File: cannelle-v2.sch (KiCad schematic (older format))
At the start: 30 parts, among them P1 USB_OTG, P2 CONN_02X04, U1 74LS157, U2 ATMEGA16U4-A, U3 SST25VF020B, U4 LD1117S12TR, U5 NCP1117ST33T3G, X1 8MHz

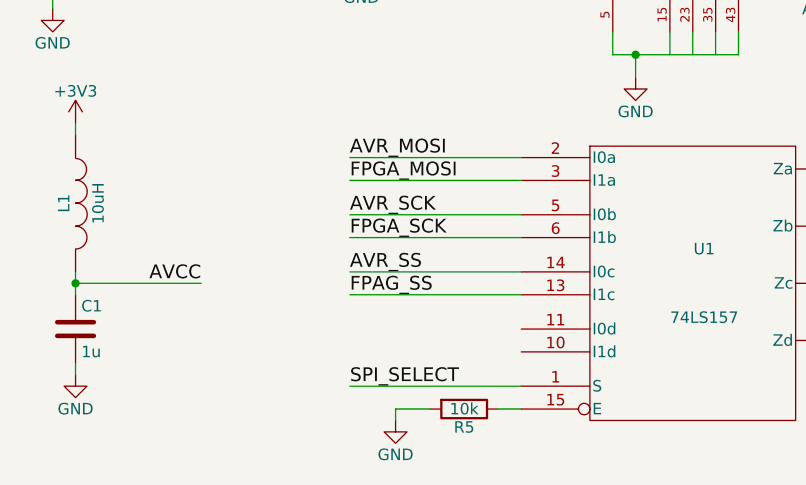
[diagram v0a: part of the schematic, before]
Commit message: Correct wrong label on schem and PCB
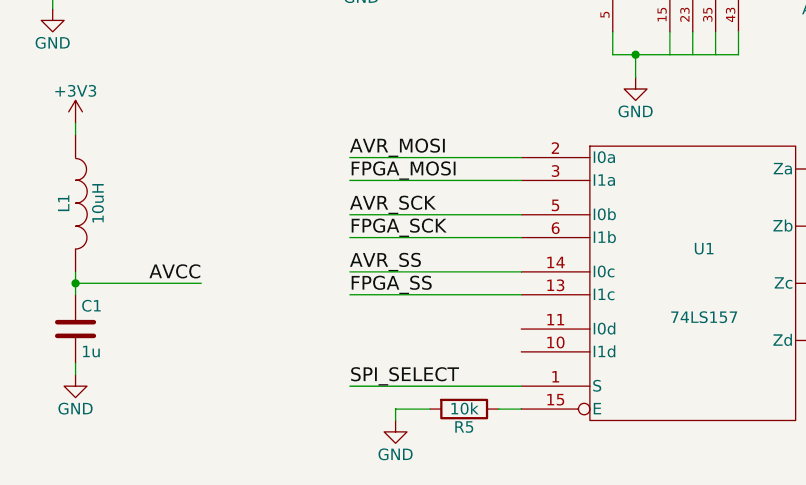
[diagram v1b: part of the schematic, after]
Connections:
- net FPAG_SS is gone; now on net FPGA_SS: U1.13 (I1c)
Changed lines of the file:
@@
 AVR_SS
 Text Label 2500 7050 0    60   ~ 0
-FPAG_SS
+FPGA_SS
 Text Label 5750 6500 2    60   ~ 0
 FLASH_MOSI

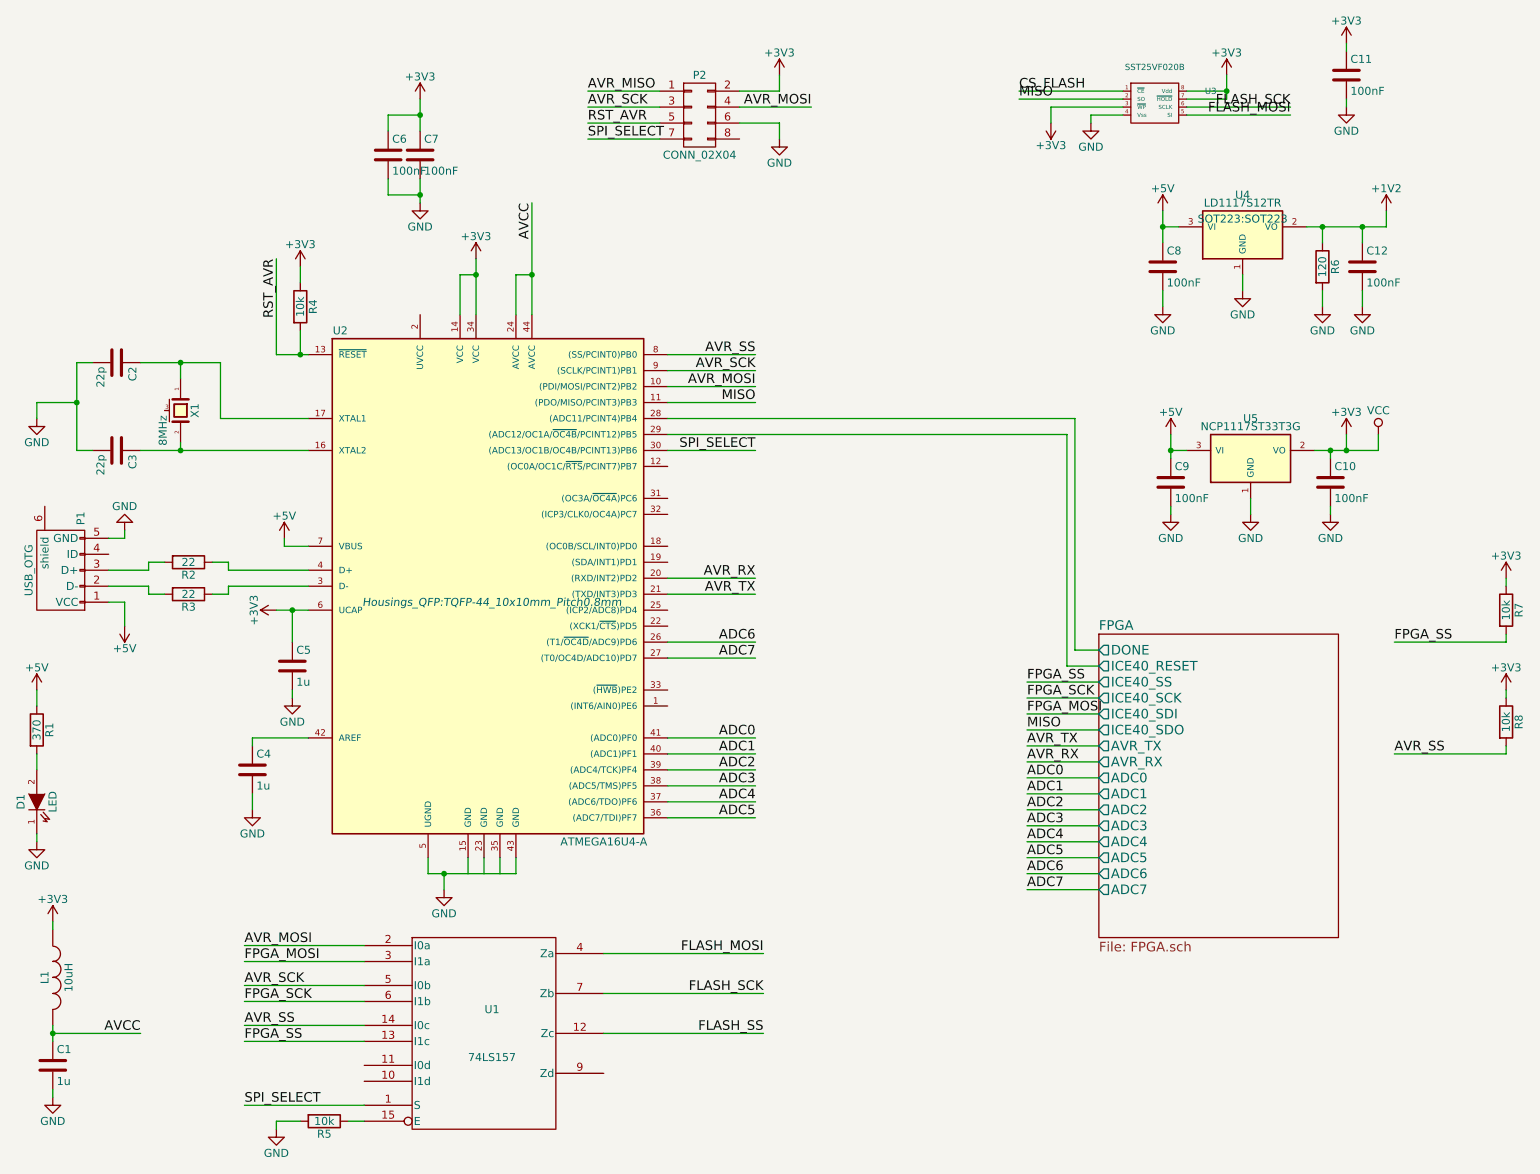
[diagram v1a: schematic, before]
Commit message: Make AtMega as only SPI Master
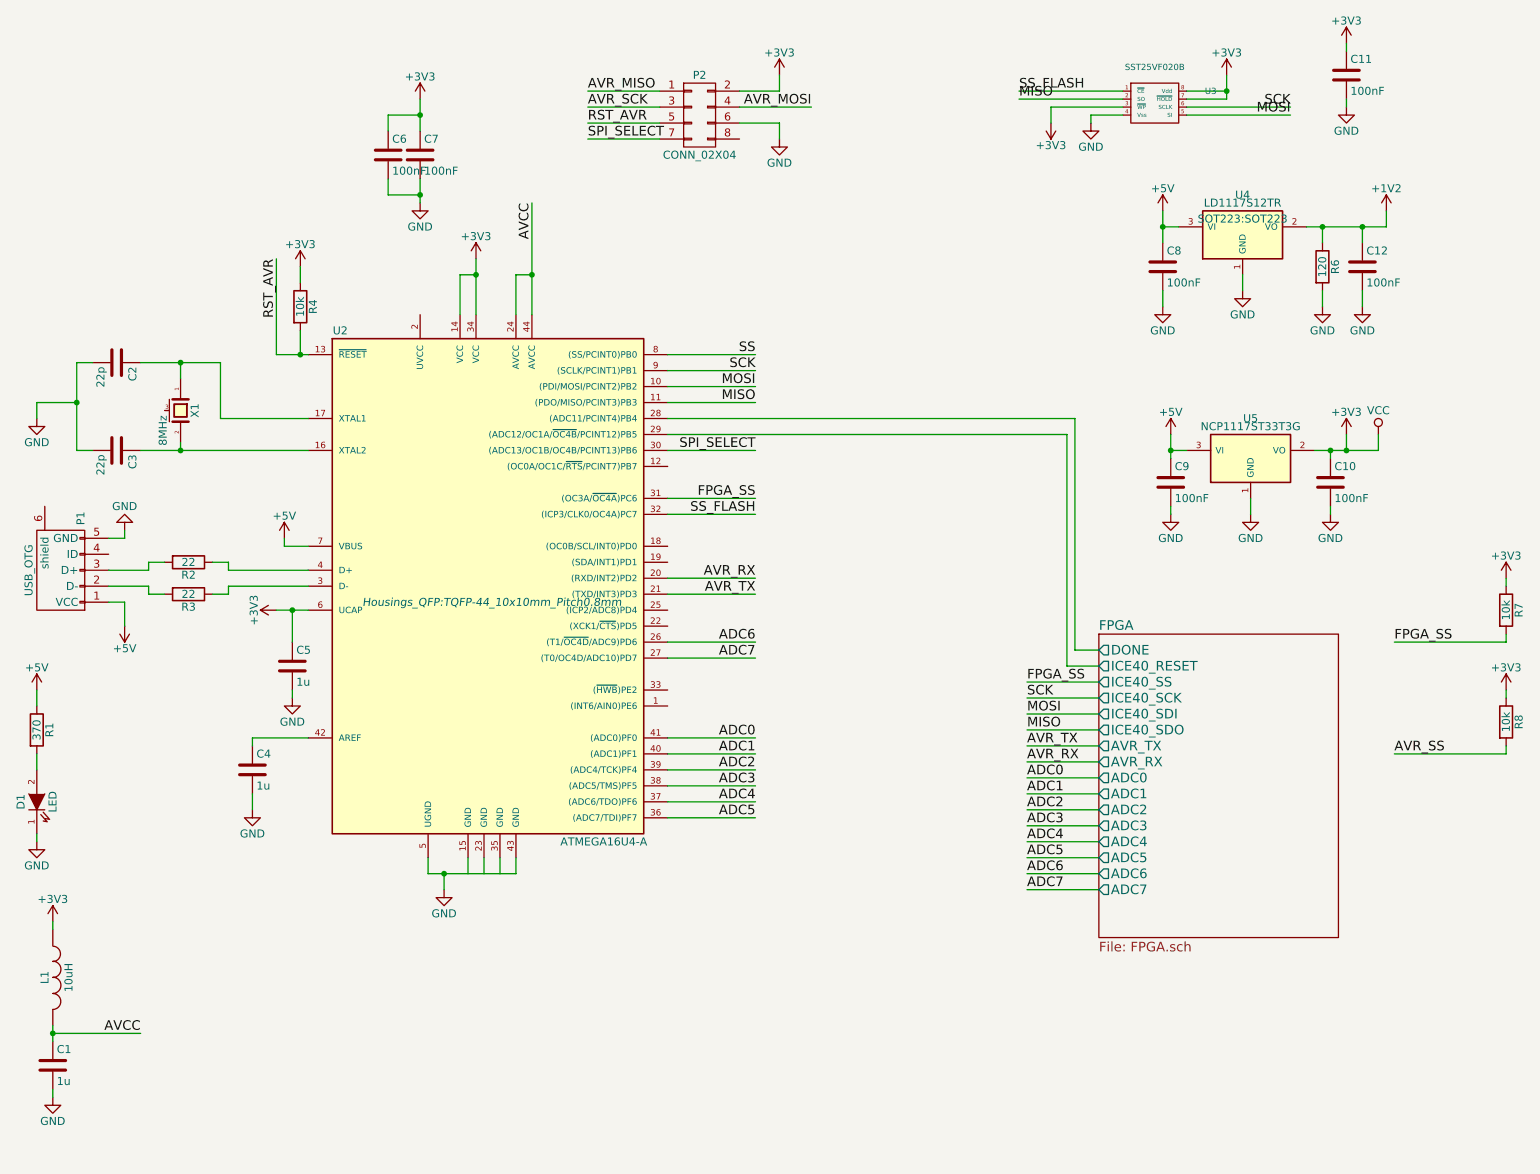
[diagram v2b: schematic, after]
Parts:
- removed R5: 10k, Resistors_SMD:R_0402, symbol R
- removed U1: 74LS157, SMD_Packages:SO-16-L, symbol 74LS157
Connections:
- net CS_FLASH is gone; now on net SS_FLASH: U3.1 (~CE)
- net AVR_MOSI: no longer U2.10 ((PDI/MOSI/PCINT2)PB2)
- net AVR_SCK: no longer U2.9 ((SCLK/PCINT1)PB1)
- net AVR_SS: no longer U2.8 ((SS/PCINT0)PB0)
- net FPGA_SS: now also U2.31 ((OC3A/~OC4A~)PC6)
- net SS_FLASH: now reaches U2.32 ((ICP3/CLK0/OC4A)PC7)
- net FLASH_MOSI renamed MOSI
- net MOSI: now also U2.10 ((PDI/MOSI/PCINT2)PB2)
- net FLASH_SCK renamed SCK
- net SCK: now also U2.9 ((SCLK/PCINT1)PB1)
- new net SS: U2.8 ((SS/PCINT0)PB0)
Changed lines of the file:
@@
 	8000 1100 7350 1100
 Text Label 7350 1100 0    60   ~ 0
-CS_FLASH
+SS_FLASH
 Wire Wire Line
 	8000 1150 7350 1150
@@
 	8400 1250 9050 1250
 Text Label 9050 1200 2    60   ~ 0
-FLASH_SCK
+SCK
 Text Label 9050 1250 2    60   ~ 0
-FLASH_MOSI
+MOSI
 Wire Wire Line
 	5150 3050 5700 3050
@@
 	5150 2950 5700 2950
 Text Label 5700 2950 2    60   ~ 0
-AVR_MOSI
+MOSI
 Wire Wire Line
 	5150 2850 5700 2850
 Text Label 5700 2850 2    60   ~ 0
-AVR_SCK
+SCK
 Wire Wire Line
 	5150 2750 5700 2750
 Text Label 5700 2750 2    60   ~ 0
-AVR_SS
+SS
 Wire Wire Line
 	5150 4150 5700 4150
@@
 FPGA_SS
 Text Label 7400 4900 0    60   ~ 0
-FPGA_SCK
+SCK
 Text Label 7400 5000 0    60   ~ 0
-FPGA_MOSI
+MOSI
 Text Label 7400 5100 0    60   ~ 0
 MISO
@@
 $EndComp
 Wire Wire Line
-	3250 6450 2500 6450
-Wire Wire Line
-	3250 6550 2500 6550
-Wire Wire Line
-	3250 6700 2500 6700
-Wire Wire Line
-	3250 6800 2500 6800
-Wire Wire Line
-	3250 6950 2500 6950
-Wire Wire Line
-	3250 7050 2500 7050
-Wire Wire Line
-	3250 7450 2500 7450
-Wire Wire Line
-	4750 6500 5750 6500
-Wire Wire Line
-	4750 6750 5750 6750
-Wire Wire Line
-	4750 7000 5750 7000
-Text Label 2500 6450 0    60   ~ 0
-AVR_MOSI
-Text Label 2500 6550 0    60   ~ 0
-FPGA_MOSI
-Text Label 2500 6700 0    60   ~ 0
-AVR_SCK
-Text Label 2500 6800 0    60   ~ 0
-FPGA_SCK
-Text Label 2500 6950 0    60   ~ 0
-AVR_SS
-Text Label 2500 7050 0    60   ~ 0
-FPGA_SS
-Text Label 5750 6500 2    60   ~ 0
-FLASH_MOSI
-Text Label 5750 6750 2    60   ~ 0
-FLASH_SCK
-Text Label 5750 7000 2    60   ~ 0
-FLASH_SS
-$Comp
-L R R5
-U 1 1 57814526
-P 3000 7550
-F 0 "R5" V 3080 7550 50  0000 C CNN
-F 1 "10k" V 3000 7550 50  0000 C CNN
-F 2 "Resistors_SMD:R_0402" V 2930 7550 50  0001 C CNN
-F 3 "" H 3000 7550 50  0000 C CNN
-	1    3000 7550
-	0    1    1    0
-$EndComp
-Wire Wire Line
-	3250 7550 3150 7550
-Wire Wire Line
-	2850 7550 2700 7550
-Wire Wire Line
-	2700 7550 2700 7600
-$Comp
-L GND #PWR030
-U 1 1 578147D3
-P 2700 7600
-F 0 "#PWR030" H 2700 7350 50  0001 C CNN
-F 1 "GND" H 2700 7450 50  0000 C CNN
-F 2 "" H 2700 7600 50  0000 C CNN
-F 3 "" H 2700 7600 50  0000 C CNN
-	1    2700 7600
-	1    0    0    -1
-$EndComp
-Text Label 2500 7450 0    60   ~ 0
-SPI_SELECT
-Wire Wire Line
 	5150 3350 5700 3350
 Text Label 5700 3350 2    60   ~ 0
 SPI_SELECT
-$Comp
-L 74LS157 U1
-U 1 1 577D8CAF
-P 4000 7000
-F 0 "U1" H 4050 7150 50  0000 C CNN
-F 1 "74LS157" H 4050 6850 50  0000 C CNN
-F 2 "SMD_Packages:SO-16-L" H 4000 7000 50  0001 C CNN
-F 3 "" H 4000 7000 50  0000 C CNN
-	1    4000 7000
-	1    0    0    -1
-$EndComp
 $Comp
 L CONN_02X04 P2
@@
 Text Label 9700 4550 0    60   ~ 0
 FPGA_SS
+Wire Wire Line
+	5150 3750 5700 3750
+Wire Wire Line
+	5150 3650 5700 3650
+Text Label 5700 3650 2    60   ~ 0
+FPGA_SS
+Text Label 5700 3750 2    60   ~ 0
+SS_FLASH
 $EndSCHEMATC

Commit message: Connect more on PCB and modify the schem a bit
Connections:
- net AVR_MISO is gone; now on net MISO: P2.1 (P1)
- net AVR_MOSI is gone; now on net MOSI: P2.4 (P4)
- net AVR_SCK is gone; now on net SCK: P2.3 (P3)
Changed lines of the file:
@@
 LIBS:contrib
 LIBS:valves
-LIBS:sst25vf020b
-LIBS:xc6slx9-tqg144
-LIBS:w_microcontrollers
 LIBS:cannelle-v2-cache
-LIBS:Oscillators
 EELAYER 25 0
 EELAYER END
@@
 $EndComp
 Text Label 4650 1100 0    60   ~ 0
-AVR_MISO
+MISO
 Text Label 4650 1200 0    60   ~ 0
-AVR_SCK
+SCK
 Text Label 4650 1300 0    60   ~ 0
 RST_AVR
 Text Label 6050 1200 2    60   ~ 0
-AVR_MOSI
+MOSI
 $Comp
 L GND #PWR02
@@
 Wire Wire Line
 	7850 5900 7400 5900
-Wire Wire Line
-	7850 6000 7400 6000
-Wire Wire Line
-	7850 6100 7400 6100
 Text Label 7400 4800 0    60   ~ 0
 FPGA_SS
@@
 Text Label 7400 5900 0    60   ~ 0
 ADC5
-Text Label 7400 6000 0    60   ~ 0
-ADC6
-Text Label 7400 6100 0    60   ~ 0
-ADC7
 Text Label 5700 5150 2    60   ~ 0
 ADC0

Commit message: Connect all pads and edge cuts
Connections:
- net RST_AVR: no longer P2.5 (P5)
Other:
- note added: "Add reset pin here\n"
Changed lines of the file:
@@
 Text Label 4650 1200 0    60   ~ 0
 SCK
-Text Label 4650 1300 0    60   ~ 0
-RST_AVR
 Text Label 6050 1200 2    60   ~ 0
 MOSI
@@
 Text Label 5700 3750 2    60   ~ 0
 SS_FLASH
+Text Notes 3750 1250 0    60   ~ 0
+Add reset pin here\n
 $EndSCHEMATC
